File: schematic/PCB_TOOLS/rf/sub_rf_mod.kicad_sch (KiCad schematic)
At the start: 39 parts, among them J4B1 Conn_01x08

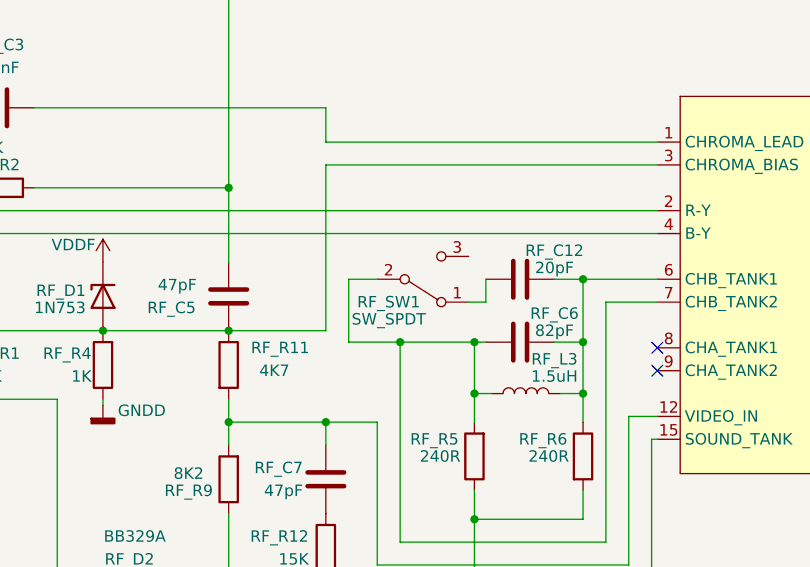
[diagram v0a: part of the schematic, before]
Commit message: fixed the switch for the sub-rf board to match the original coleco for chan 3/4 selection
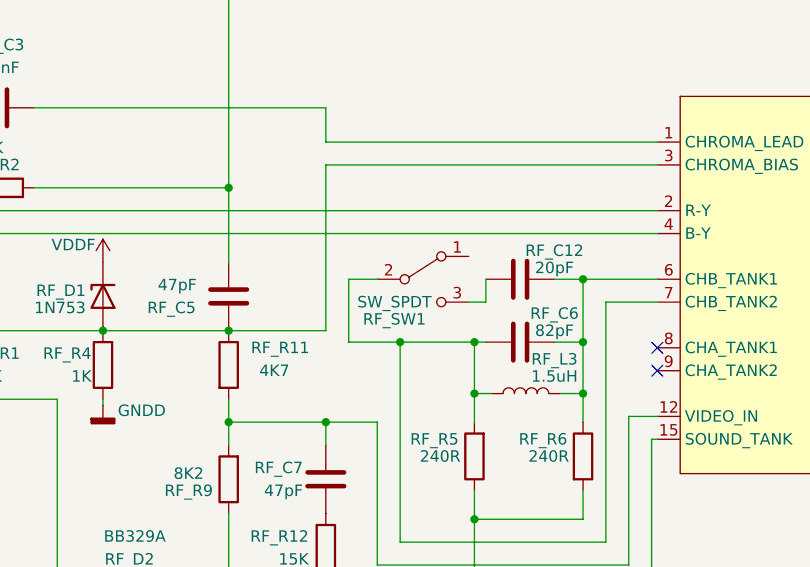
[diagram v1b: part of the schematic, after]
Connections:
- net at RF_C12.1: now also RF_SW1.3 (C); no longer RF_SW1.1 (A)
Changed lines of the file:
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@@
     (pin "1")
   )
-  (symbol (lib_id "Switch:SW_SPDT") (at 108.585 92.075 0) (mirror x) (unit 1)
+  (symbol (lib_id "Switch:SW_SPDT") (at 108.585 92.075 0) (unit 1)
     (in_bom yes) (on_board yes)
-    (property "Reference" "RF_SW1" (id 0) (at 104.775 94.615 0))
-    (property "Value" "SW_SPDT" (id 1) (at 104.775 96.52 0))
+    (property "Reference" "RF_SW1" (id 0) (at 105.41 96.52 0))
+    (property "Value" "SW_SPDT" (id 1) (at 105.41 94.615 0))
     (property "Footprint" "1101M2S3ABE2:1101M2S3ABE2" (id 2) (at 108.585 92.075 0)
       (effects (font (size 1.27 1.27)) hide)
